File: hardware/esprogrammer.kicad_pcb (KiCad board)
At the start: 2 copper layers, 45 x 20.5 mm, 25 parts, among them P1 USB_OTG, P2 CONN_02X03, Q1 MMBT3904, Q2 MMBT3904, SW1 SW_PUSH, SW2 SW_PUSH, U1 AP1117, U2 CP2102

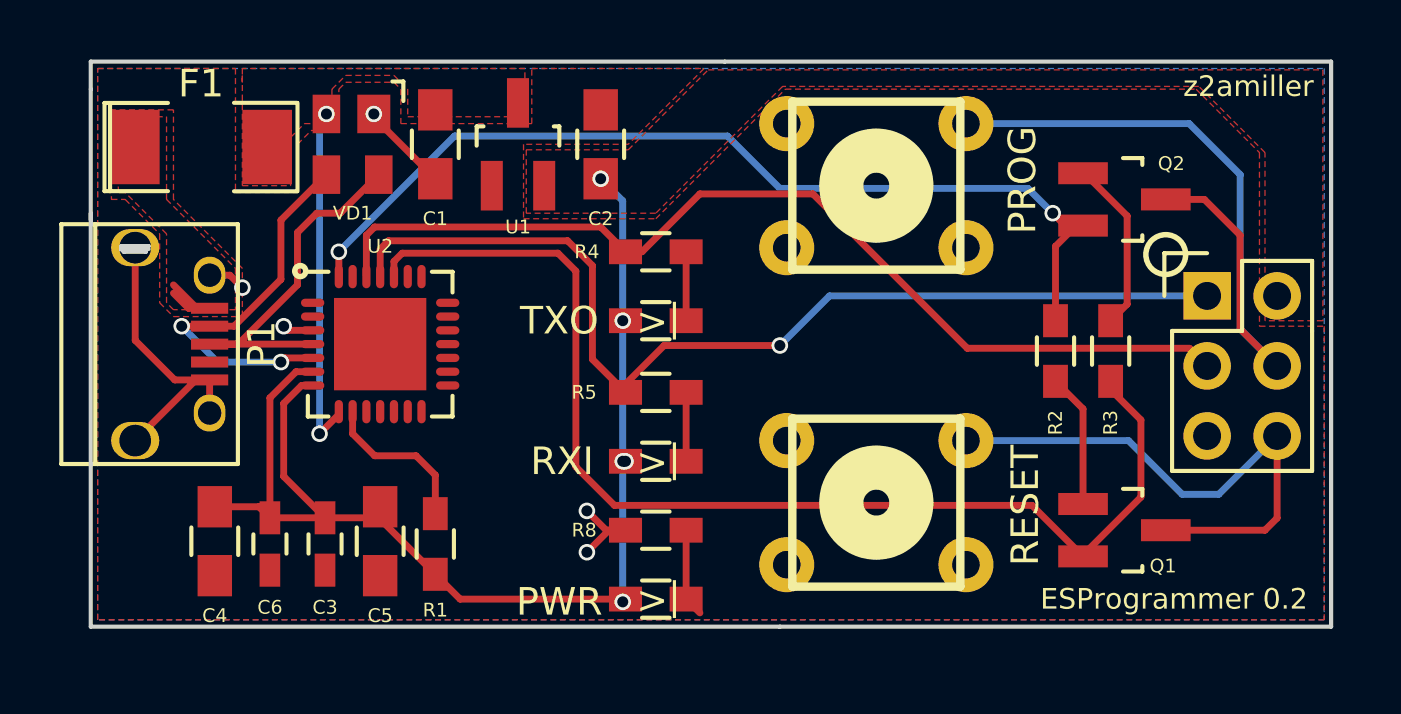
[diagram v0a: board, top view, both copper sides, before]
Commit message: Re-center some parts, bigger 3v3 traces.
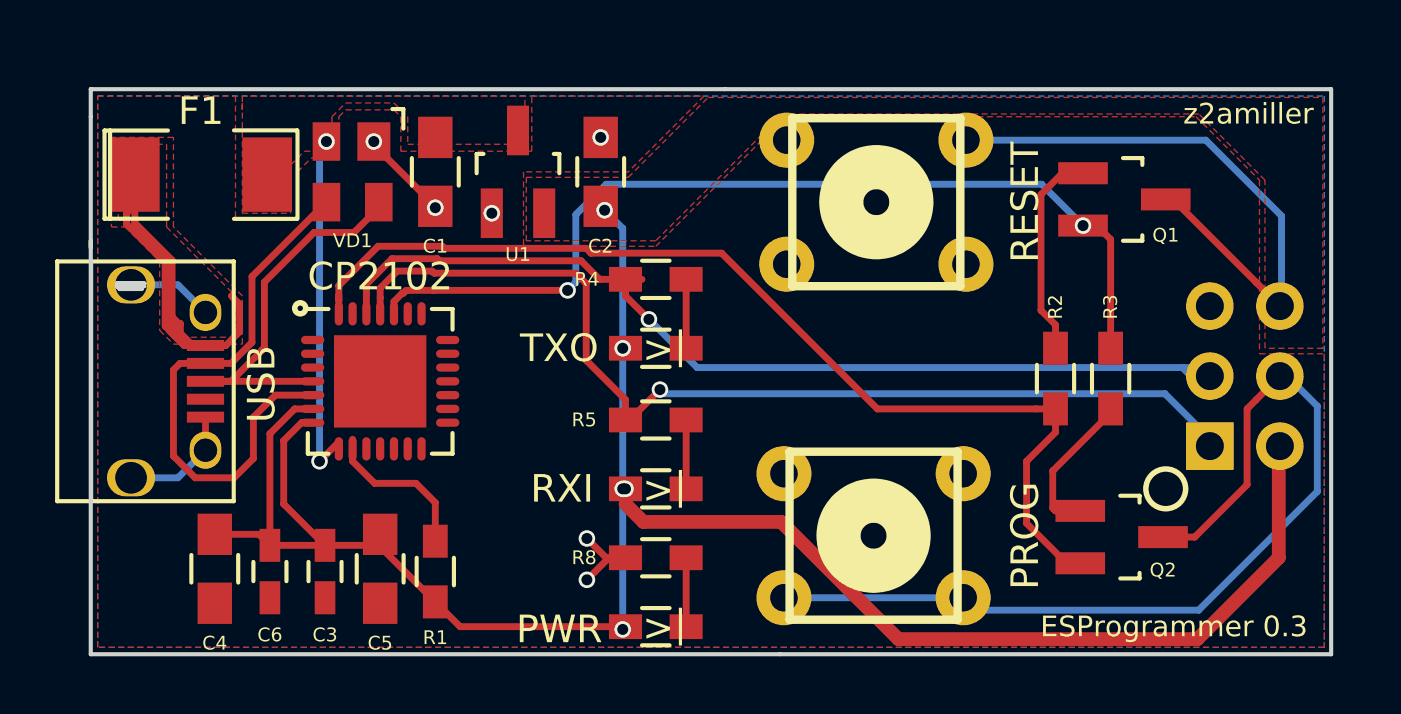
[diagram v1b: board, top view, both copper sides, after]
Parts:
- P2: moved to B.Cu
- moved SW1 12.7 mm to (187.4, 103.7), turned to 90 degrees
- moved Q2 12.3 mm to (196.4, 103.8)
- moved Q1 12.0 mm to (196.5, 91.5)
- moved SW2 10.9 mm to (187.5, 91.6)
- moved P2 5.45 mm to (199.6, 100.5)
- moved P1 1.36 mm to (161.6, 98.1)
- moved U2 1.35 mm to (169.5, 98.1)
- moved C1 1.00 mm to (171.5, 90.5)
- moved C2 1.00 mm to (177.5, 90.5)
- moved C3 1.00 mm to (167.5, 105.0)
- moved C4 1.00 mm to (163.5, 104.9)
- moved C5 1.00 mm to (169.5, 104.9)
- moved C6 1.00 mm to (165.5, 105.0)
- moved D1 1.00 mm to (179.5, 96.9)
- moved D2 1.00 mm to (179.5, 102.0)
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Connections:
- SW1 pad 3: (no net) -> ESP_GPIO0
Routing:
- net +3V3: track 45.4 -> 76.4 mm
- net Net-(F1-Pad1): track 3.20 -> 20.6 mm
- net ESP_GPIO0: track 26.7 -> 34.7 mm
- net RTS: track 42.1 -> 34.9 mm, vias 0 -> 2
- net D-: track 14.1 -> 20.1 mm, vias 2 -> 0
- net GND: track 20.8 -> 15.4 mm, vias 5 -> 6
- net Net-(Q1-Pad1): track 4.86 -> 7.47 mm
- net DTR: track 35.0 -> 37.4 mm, vias 2 -> 0
- net ESP_RST: track 20.2 -> 22.0 mm
- net D+: track 13.5 -> 14.4 mm
- net TXD: track 36.9 -> 36.1 mm, vias 0 -> 1
- net Net-(D5-Pad1): track 3.21 -> 2.50 mm
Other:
- outline, holes or cut-outs redrawn
- net class 3v3 added: clearance 0.2, trace_width 0.5, via_dia 0.8, via_drill 0.4
- board text added: "CP2102"
- board text added: "ESProgrammer 0.3"
- board text added: "USB"
- board text removed: "ESProgrammer 0.2"

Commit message: Update silkscreened version.
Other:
- board text added: "ESProgrammer 0.4"
- board text removed: "ESProgrammer 0.3"
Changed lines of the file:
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@@
     (arrow2b (pts (xy 217.835405 87.533623) (xy 218.419076 88.661554)))
   )
-  (gr_text "ESProgrammer 0.3" (at 198.3 107) (layer F.SilkS)
+  (gr_text "ESProgrammer 0.4" (at 198.3 107) (layer F.SilkS)
     (effects (font (size 0.75 0.75) (thickness 0.15)))
   )
@@
   (segment (start 166 102.55) (end 166 100.25) (width 0.25) (layer F.Cu) (net 3))
   (segment (start 177.941948 92.191948) (end 177.641949 91.891949) (width 0.25) (layer B.Cu) (net 3))
-  (segment (start 178.3 96.9) (end 178.3 92.55) (width 0.25) (layer B.Cu) (net 3))
-  (segment (start 178.3 92.55) (end 177.941948 92.191948) (width 0.25) (layer B.Cu) (net 3))
+  (segment (start 178.3 96.9) (end 178.3 92.55) (width 0.5) (layer B.Cu) (net 3))
+  (segment (start 178.3 92.55) (end 177.941948 92.191948) (width 0.5) (layer B.Cu) (net 3))
   (via (at 177.641949 91.891949) (size 0.6) (drill 0.4) (layers F.Cu B.Cu) (net 3))
   (segment (start 202.1 104.5) (end 202.1 100.14) (width 0.5) (layer F.Cu) (net 3) (status 20))
@@
   (segment (start 178.3 107.1) (end 178.4 107) (width 0.25) (layer F.Cu) (net 3) (status 30))
   (via (at 178.3 107.1) (size 0.6) (drill 0.4) (layers F.Cu B.Cu) (net 3) (status 30))
-  (segment (start 178.3 102.1) (end 178.3 107.1) (width 0.25) (layer B.Cu) (net 3))
+  (segment (start 178.3 102.1) (end 178.3 107.1) (width 0.5) (layer B.Cu) (net 3))
   (segment (start 178.4 102) (end 178.3 102.1) (width 0.25) (layer B.Cu) (net 3))
-  (segment (start 178.3 96.9) (end 178.3 102) (width 0.25) (layer B.Cu) (net 3))
+  (segment (start 178.3 96.9) (end 178.3 102) (width 0.5) (layer B.Cu) (net 3))
   (via (at 178.3 102) (size 0.6) (drill 0.4) (layers F.Cu B.Cu) (net 3) (status 30))
   (segment (start 178.4 97) (end 178.3 96.9) (width 0.25) (layer F.Cu) (net 3) (status 30))

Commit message: Fix 3v3 fill, add some gnd vias.
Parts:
- added REF**: SolderWirePad_single_0-8mmDrill, Wire_Connections_Bridges:small_via, F.Cu at (166.2, 94.9)
- added REF**: SolderWirePad_single_0-8mmDrill, Wire_Connections_Bridges:small_via, F.Cu at (179.3, 88.5)
- added REF**: SolderWirePad_single_0-8mmDrill, Wire_Connections_Bridges:small_via, F.Cu at (173.6, 101.2)
- added REF**: SolderWirePad_single_0-8mmDrill, Wire_Connections_Bridges:small_via, F.Cu at (173.6, 96.2)
- added REF**: SolderWirePad_single_0-8mmDrill, Wire_Connections_Bridges:small_via, F.Cu at (196.3, 101.2)
- moved SW2 0.07 mm to (187.5, 91.5)
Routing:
- net +3V3: track 76.4 -> 44.7 mm, vias 5 -> 3
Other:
- net class 3v3 removed
- board text added: "3v3"
- board text added: "GND"
- board text added: "RST"
- board text added: "RX"
- board text added: "TX"

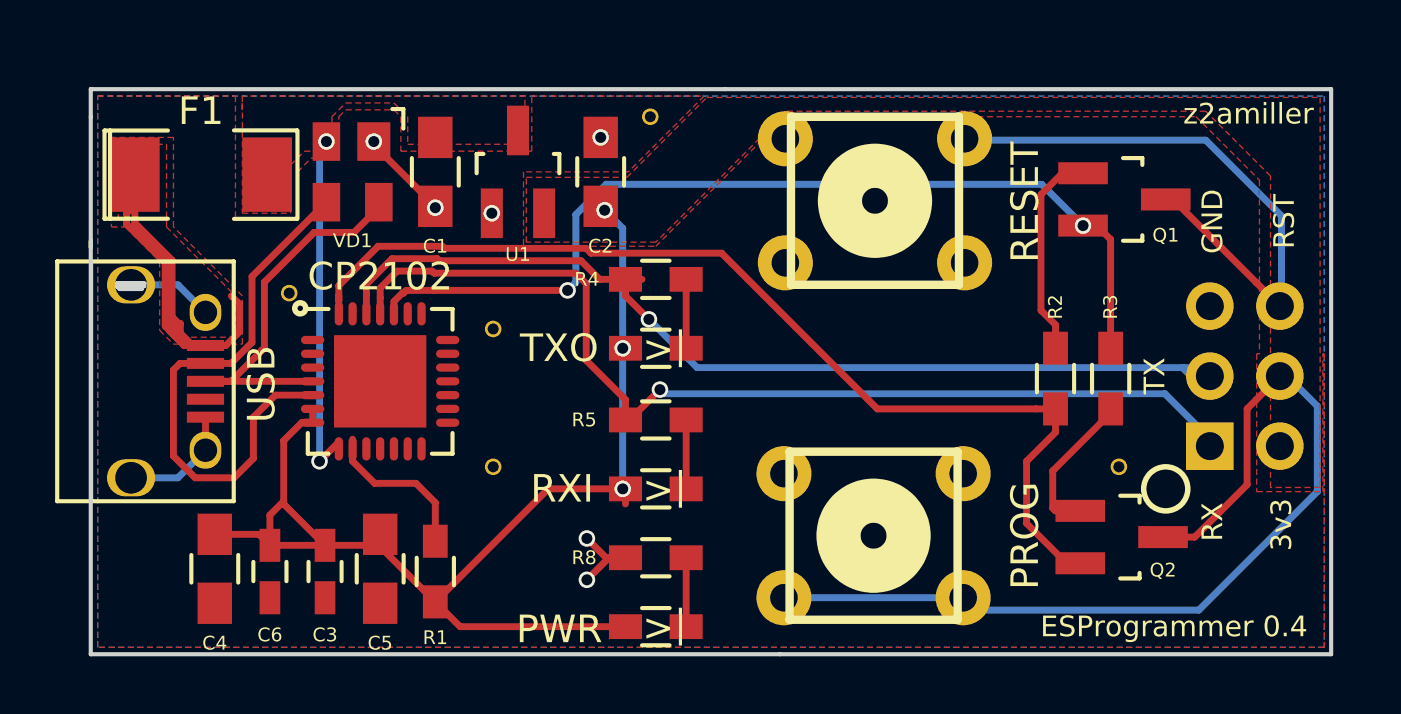
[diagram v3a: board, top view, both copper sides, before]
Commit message: Improve via placement.
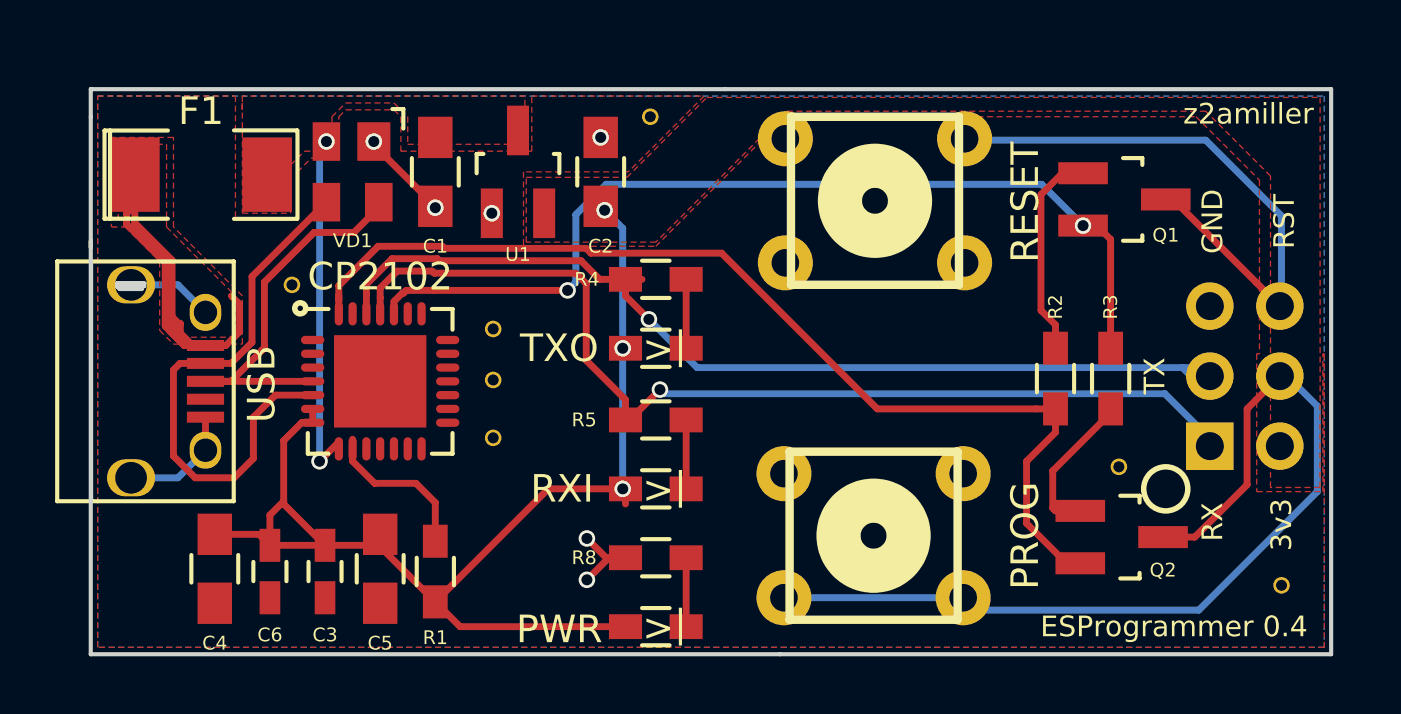
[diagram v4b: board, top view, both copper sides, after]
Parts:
- added REF**: SolderWirePad_single_0-8mmDrill, Wire_Connections_Bridges:small_via, F.Cu at (202.2, 105.5)
- added REF**: SolderWirePad_single_0-8mmDrill, Wire_Connections_Bridges:small_via, F.Cu at (173.6, 98.0)
- moved REF** 1.05 mm to (173.6, 100.2)
- moved REF** 0.32 mm to (166.3, 94.6)
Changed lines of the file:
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@@
 (kicad_pcb (version 4) (host pcbnew 4.0.3-rc7-stable)
   (general
-    (links 64)
+    (links 66)
     (no_connects 0)
     (area 158.924999 87.424999 204.075001 108.075001)
@@
     (tracks 217)
     (zones 0)
-    (modules 30)
+    (modules 32)
     (nets 37)
   )
@@
   )
   (module Wire_Connections_Bridges:small_via (layer F.Cu)
-    (at 166.2 94.9)
+    (at 202.2 105.5)
+    (fp_text reference REF** (at 0 -2.54) (layer F.SilkS) hide
+      (effects (font (size 1 1) (thickness 0.15)))
+    )
+    (fp_text value SolderWirePad_single_0-8mmDrill (at 0 2.54) (layer F.Fab) hide
+      (effects (font (size 1 1) (thickness 0.15)))
+    )
+    (pad 1 thru_hole circle (at 0 0) (size 0.6 0.6) (drill 0.4) (layers *.Cu)
+      (net 2 GND) (zone_connect 2))
+  )
+  (module Wire_Connections_Bridges:small_via (layer F.Cu)
+    (at 173.6 98.05)
+    (fp_text reference REF** (at 0 -2.54) (layer F.SilkS) hide
+      (effects (font (size 1 1) (thickness 0.15)))
+    )
+    (fp_text value SolderWirePad_single_0-8mmDrill (at 0 2.54) (layer F.Fab) hide
+      (effects (font (size 1 1) (thickness 0.15)))
+    )
+    (pad 1 thru_hole circle (at 0 0) (size 0.6 0.6) (drill 0.4) (layers *.Cu)
+      (net 2 GND) (zone_connect 2))
+  )
+  (module Wire_Connections_Bridges:small_via (layer F.Cu)
+    (at 166.3 94.6)
     (fp_text reference REF** (at 0 -2.54) (layer F.SilkS) hide
       (effects (font (size 1 1) (thickness 0.15)))
@@
   )
   (module Wire_Connections_Bridges:small_via (layer F.Cu)
-    (at 173.6 101.2)
+    (at 173.6 100.15)
     (zone_connect 2)
     (fp_text reference REF** (at 0 -2.54) (layer F.SilkS) hide

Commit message: Shrink board for v0.5
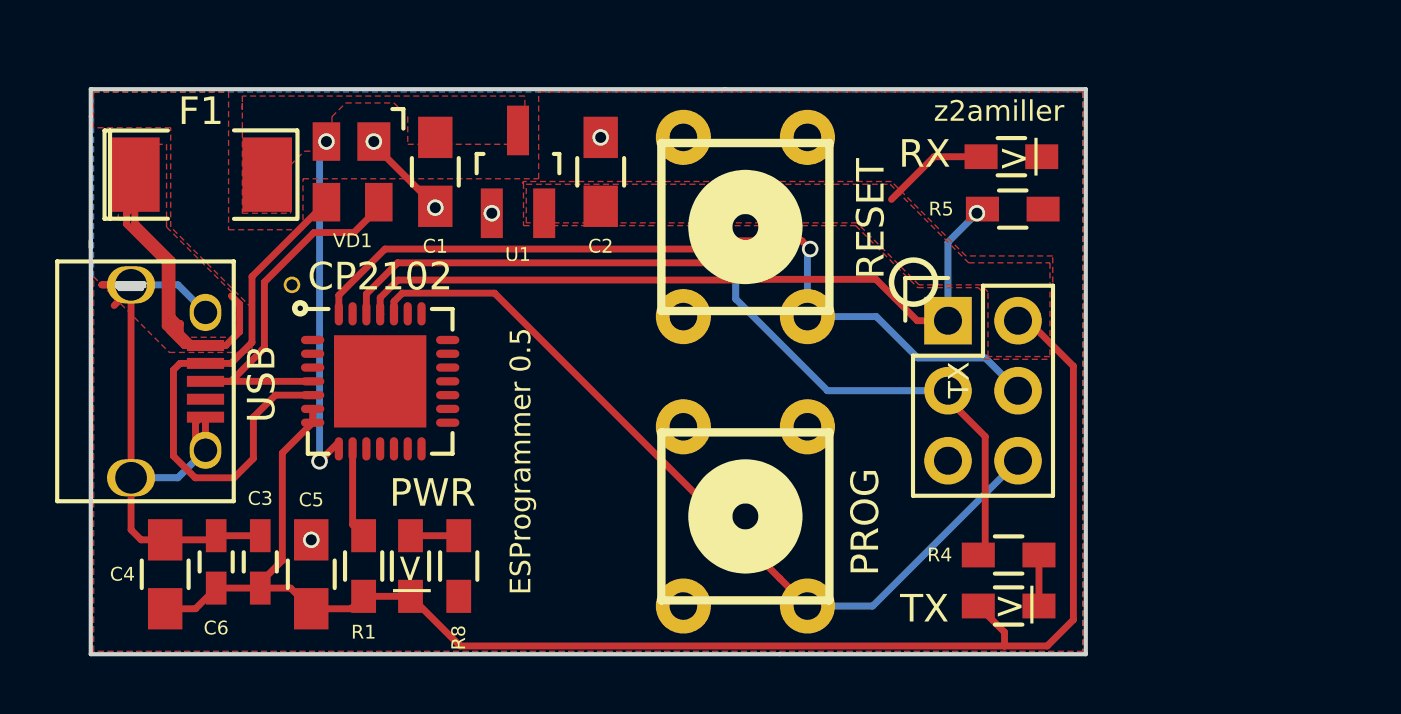
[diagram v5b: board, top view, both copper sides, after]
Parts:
- removed Q1, Q2: MMBT3904, TO_SOT_Packages_SMD:SOT-23_Handsoldering
- removed R2, R3: 10k, Resistors_SMD:R_0603_HandSoldering
- removed the REF** at (202.2, 105.5)
- removed the REF** at (173.6, 98.0)
- removed the REF** at (179.3, 88.5)
- removed the REF** at (173.6, 100.2)
- removed the REF** at (173.6, 96.2)
- removed the REF** at (196.3, 101.2)
- P2: moved to F.Cu
- moved D2 17.7 mm to (192.4, 90.0)
- moved R4 16.2 mm to (192.3, 104.4)
- moved D1 15.9 mm to (192.3, 106.2)
- moved R5 15.0 mm to (192.4, 91.8)
- moved SW2 12.4 mm to (182.8, 103.0), turned to 180 degrees
- moved SW1 12.1 mm to (182.8, 92.5), turned to 180 degrees
- moved P2 10.5 mm to (190.1, 95.9)
- moved D5 9.17 mm to (170.6, 104.8), turned to 270 degrees
- moved R8 7.16 mm to (172.3, 104.8), turned to 270 degrees
- moved R1 2.61 mm to (168.9, 104.8)
- moved C5 2.51 mm to (167.0, 105.1), turned to 90 degrees
- moved C3 2.38 mm to (165.2, 104.7), turned to 90 degrees
- moved C6 1.98 mm to (163.6, 104.7), turned to 90 degrees
- moved C4 1.81 mm to (161.7, 105.1), turned to 90 degrees
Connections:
- P2 pad 4: ESP_GPIO0 -> DTR
- SW1 pad 1: ESP_GPIO0 -> DTR
- SW1 pad 3: ESP_GPIO0 -> (no net)
- SW1 pad 4: GND -> (no net)
- SW2 pad 4: GND -> (no net)
- U2 pad 24: RTS -> ESP_RST
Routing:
- net RTS: track 34.9 -> 0.00 mm, vias 2 -> 0
- net ESP_GPIO0: track 34.7 -> 0.00 mm
- net GND: track 15.4 -> 30.6 mm, vias 6 -> 5
- net +3V3: track 44.7 -> 59.8 mm, vias 3 -> 0
- net RXD: track 37.0 -> 26.7 mm
- net ESP_RST: track 22.0 -> 30.1 mm
- net Net-(Q1-Pad1): track 7.47 -> 0.00 mm
- net DTR: track 37.4 -> 30.0 mm, vias 0 -> 1
- net Net-(Q2-Pad1): track 5.81 -> 0.00 mm
- net TXD: track 36.1 -> 31.6 mm
- net Net-(R1-Pad2): track 5.82 -> 3.32 mm
- net Net-(D2-Pad1): track 2.50 -> 0.00 mm
- net Net-(D5-Pad1): track 2.50 -> 1.75 mm
- net Net-(D1-Pad1): track 2.50 -> 1.85 mm
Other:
- board size 45 x 20.5 mm -> 36.1 x 20.5 mm
- board text added: "ESProgrammer 0.5"
- board text removed: "3v3"
- board text removed: "ESProgrammer 0.4"
- board text removed: "GND"
- board text removed: "RST"
- board text removed: "RXI"
- board text removed: "TXO"
